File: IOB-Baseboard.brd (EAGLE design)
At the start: 106 x 100 mm, 21 parts

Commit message: added mounting holes
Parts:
- added U$3, U$4, U$5: MOUNTINGHOLE, SPCoast:MOUNTINGHOLE
- moved U$1 45.3 mm to (51.4, 85.2), turned to 0 degrees
- moved R18 11.5 mm to (6.22, 74.9), turned to 180 degrees
- moved LED18 9.25 mm to (6.22, 77.5)
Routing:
- net VIN: track 495.9 -> 484.3 mm
- net GND: track 45.1 -> 46.1 mm

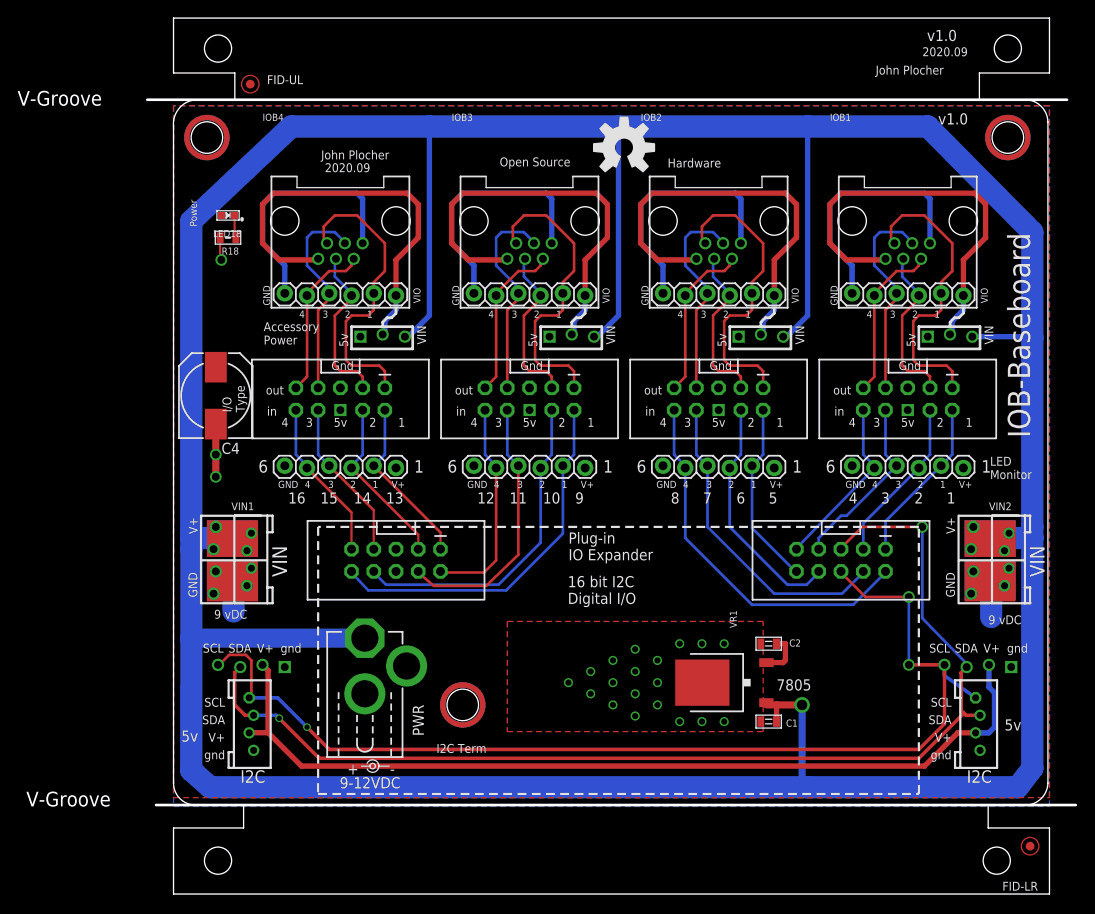
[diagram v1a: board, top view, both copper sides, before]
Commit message: put LEDS back on board, move 2x5 personal;ity and VIO connectors
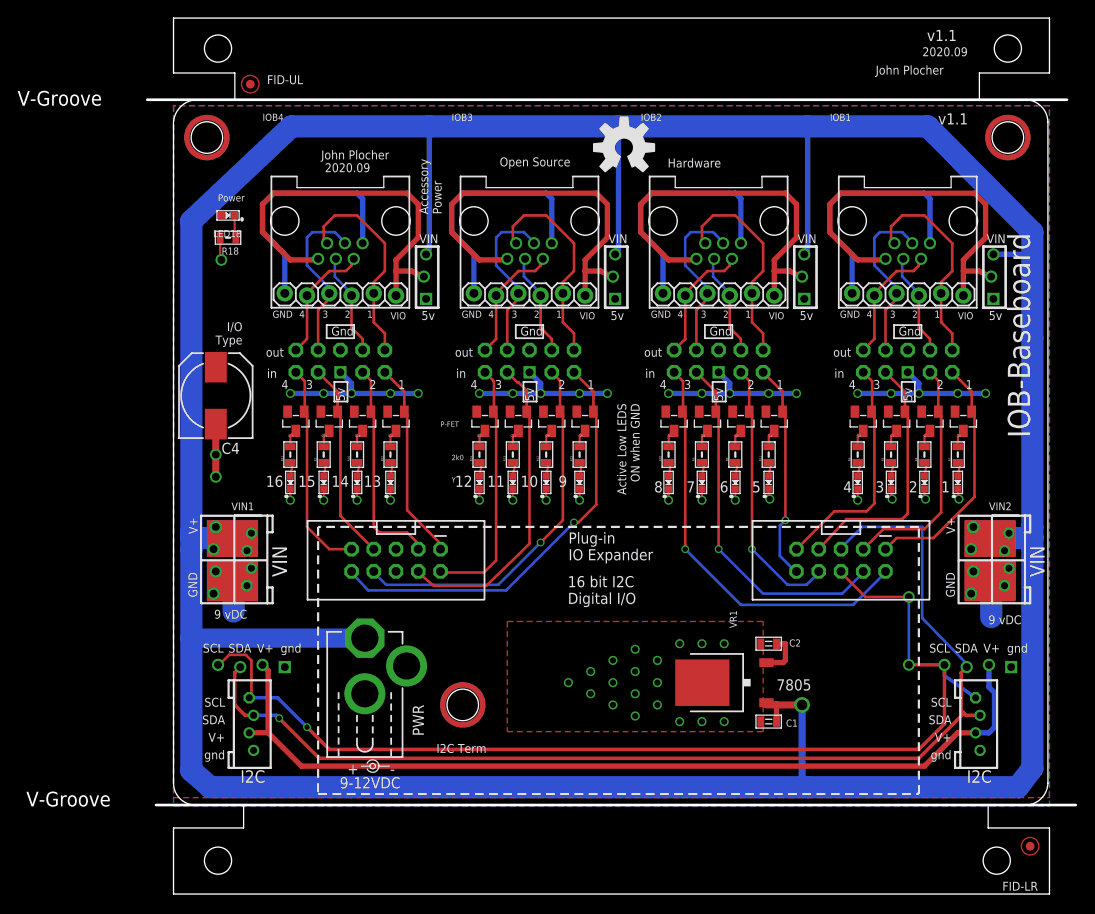
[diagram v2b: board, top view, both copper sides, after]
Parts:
- added LED10, LED11, LED12, LED13, LED14, LED15, LED17, LED19, LED2, LED3, LED4, LED5, LED6, LED7, LED8, LED9: Y, SPCoast:0603-LED
- added Q0, Q1, Q10, Q11, Q12, Q13, Q14, Q15, Q2, Q3, Q4, Q5, Q6, Q7, Q8, Q9: P-FET, SPCoast:SOT23
- added R10, R11, R12, R13, R14, R15, R16, R2, R21, R22, R4, R5, R6, R7, R8, R9: 2K0, SPCoast:0805-RES
- IOB1, IOB2, IOB3, IOB4: device SPCoast:IOB-V3 -> SPCoast:IOB-V3-BASE
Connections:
- new net N$10: LED8.A, R10.1
- new net N$11: Q8.3, R15.2
- new net N$12: Q9.3, R12.2
- new net N$13: Q10.3, R13.2
- new net N$14: Q11.3, R14.2
- new net N$15: LED13.A, R15.1
- new net N$16: LED10.A, R12.1
- new net N$23: LED11.A, R13.1
- new net N$24: LED12.A, R14.1
- new net N$28: Q12.3, R22.2
- new net N$29: Q13.3, R16.2
- new net N$3: Q4.3, R11.2
- new net N$30: Q14.3, R2.2
- new net N$31: Q15.3, R21.2
- new net N$32: LED19.A, R22.1
- new net N$33: LED14.A, R16.1
- new net N$34: LED15.A, R2.1
- new net N$35: LED17.A, R21.1
- new net N$4: Q5.3, R8.2
- new net N$44: Q0.3, R7.2
- new net N$45: Q1.3, R4.2
- new net N$46: Q2.3, R5.2
- new net N$47: Q3.3, R6.2
- new net N$48: LED5.A, R7.1
- new net N$49: LED2.A, R4.1
- new net N$5: Q6.3, R9.2
- new net N$50: LED3.A, R5.1
- new net N$51: LED4.A, R6.1
- new net N$6: Q7.3, R10.2
- new net N$7: LED9.A, R11.1
- new net N$8: LED6.A, R8.1
- new net N$9: LED7.A, R9.1
- net GND: now also LED10.C, LED11.C, LED12.C, LED13.C, LED14.C, LED15.C, LED17.C, LED19.C, LED2.C, LED3.C, LED4.C, LED5.C, LED6.C, LED7.C, LED8.C, LED9.C; no longer IOB1.GND@4, IOB2.GND@4, IOB3.GND@4, IOB4.GND@4
- net P1: now also Q0.1; no longer IOB1.I1@1
- net P10: now also Q9.1; no longer IOB3.I2@1
- net P11: now also Q10.1; no longer IOB3.I3@1
- net P12: now also Q11.1; no longer IOB3.I4@1
- net P13: now also Q12.1; no longer IOB4.I1@1
- net P14: now also Q13.1; no longer IOB4.I2@1
- net P15: now also Q14.1; no longer IOB4.I3@1
- net P16: now also Q15.1; no longer IOB4.I4@1
- net P2: now also Q1.1; no longer IOB1.I2@1
- net P3: now also Q2.1; no longer IOB1.I3@1
- net P4: now also Q3.1; no longer IOB1.I4@1
- net P5: now also Q4.1; no longer IOB2.I1@1
- net P6: now also Q5.1; no longer IOB2.I2@1
- net P7: now also Q6.1; no longer IOB2.I3@1
- net P8: now also Q7.1; no longer IOB2.I4@1
- net P9: now also Q8.1; no longer IOB3.I1@1
- net VCC: now also Q0.2, Q1.2, Q10.2, Q11.2, Q12.2, Q13.2, Q14.2, Q15.2, Q2.2, Q3.2, Q4.2, Q5.2, Q6.2, Q7.2, Q8.2, Q9.2; no longer IOB1.5V@4, IOB2.5V@4, IOB3.5V@4, IOB4.5V@4
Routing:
- net VCC: track 5.17 -> 80.8 mm, vias 0 -> 20
- net VIN: track 484.3 -> 459.9 mm
- net GND: track 46.1 -> 66.3 mm, vias 22 -> 38
- net P1: track 12.2 -> 27.9 mm
- net P3: track 13.6 -> 29.1 mm
- net P2: track 11.9 -> 27.2 mm
- net P4: track 13.0 -> 26.8 mm
- net P9: track 35.6 -> 49.2 mm, vias 0 -> 1
- net P16: track 11.4 -> 24.4 mm
- net P8: track 35.7 -> 48.2 mm, vias 0 -> 1
- net P10: track 30.3 -> 42.8 mm, vias 0 -> 1
- net P11: track 23.7 -> 36.0 mm
- net P14: track 12.4 -> 24.7 mm
- net P7: track 29.0 -> 41.0 mm, vias 0 -> 1
- net P12: track 17.5 -> 29.2 mm
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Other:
- board text added: "2k0"
- board text added: ">DRAWING_NAME"
- board text added: "Active Low LEDS ON when GND"
- board text added: "Made in the Coast Division, PCR, NMRA"
- board text added: "Model Railroading is Fun!"
- board text added: "P-FET"
- board text added: "Y"
- board text added: "v1.1"
- board text removed: "1.0 - experimental platform for plug in I/O interface, LED monitor and I2C chip carriers"
- board text removed: "5v"
- board text removed: "I2C-7313-IOB"
- board text removed: "LED Monitor"
- board text removed: "v1.0"

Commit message: update version text
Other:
- board text added: "v1.0"
- board text removed: "v1.1"
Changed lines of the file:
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@@
 <board>
 <plain>
-<text x="87.28339375" y="87.855534375" size="1.27" layer="21" rot="SR0">v1.1</text>
+<text x="87.28339375" y="87.855534375" size="1.27" layer="21" rot="SR0">v1.0</text>
 <text x="2.2548" y="40.2418" size="1.4224" layer="22" font="vector" ratio="15" rot="MR270">www. SP Coast .com</text>
 <text x="36.9627" y="83.2992" size="1.4224" layer="22" font="vector" ratio="15" rot="MR180">16 bit (4x IO4 ports)
@@
 <text x="45.085" y="38.1" size="1.27" layer="21" rot="SR0">Plug-in
 IO Expander</text>
-<text x="86.01339375" y="97.380534375" size="1.27" layer="21" rot="SR0">v1.1</text>
+<text x="86.01339375" y="97.380534375" size="1.27" layer="21" rot="SR0">v1.0</text>
 <text x="85.48799375" y="95.645009375" size="1.016" layer="21">2020.09</text>
 <text x="87.63" y="45.847" size="1.27" layer="21">1</text>

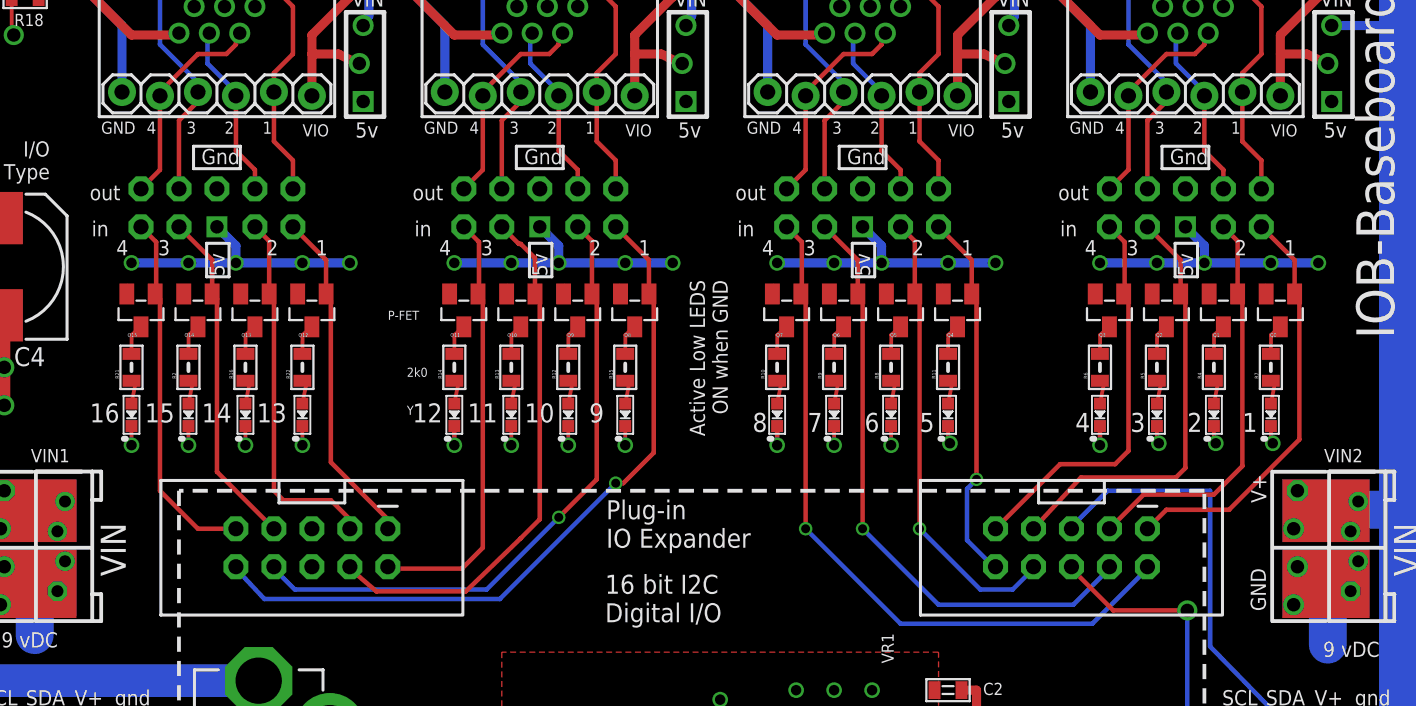
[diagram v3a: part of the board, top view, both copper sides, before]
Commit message: added values for connectors
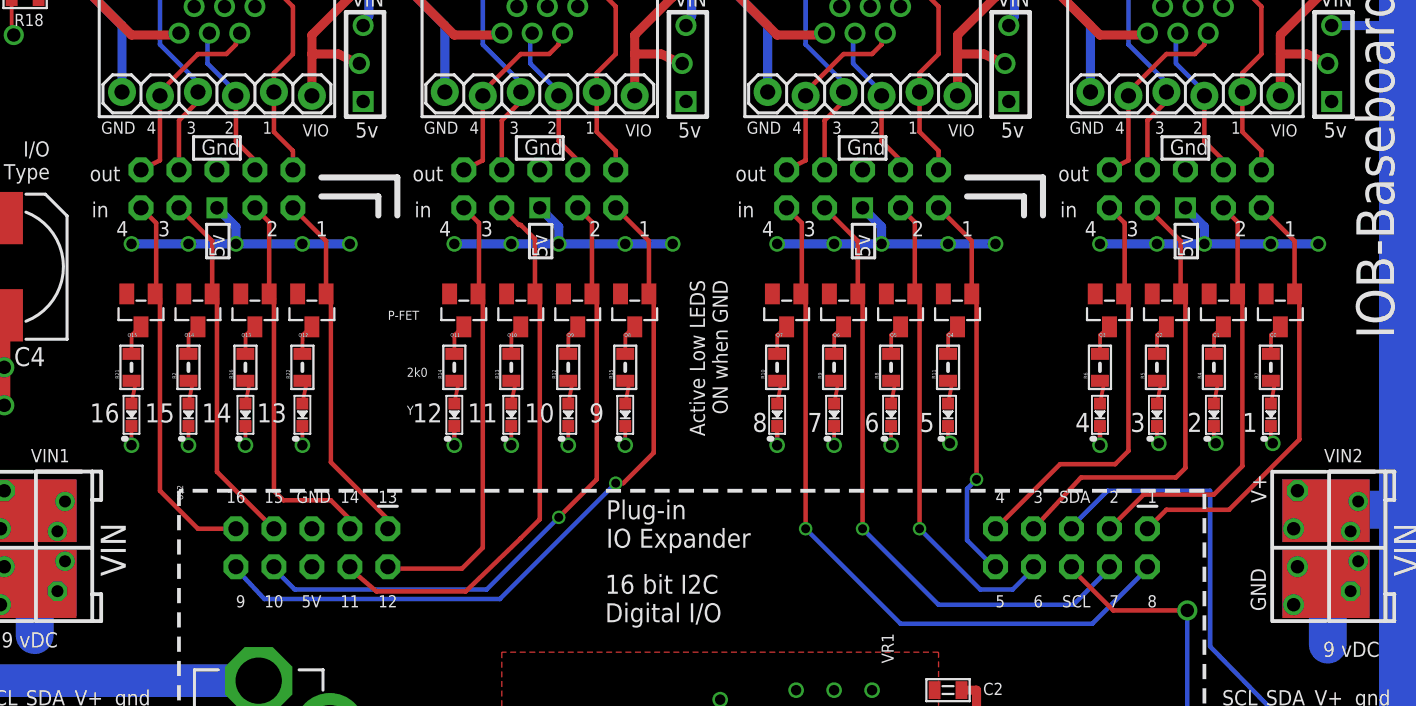
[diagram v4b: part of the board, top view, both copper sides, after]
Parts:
- J1, J2: value (none) -> I2C
- PWR: value (none) -> 2.1mm
- U$2: value I2C-EXPANDER -> CONNECTOR-I2C-EXPANDER
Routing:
- net P11: track 36.0 -> 37.3 mm
- net P10: track 42.8 -> 44.0 mm
- net P12: track 29.2 -> 30.5 mm
- net P9: track 49.2 -> 50.4 mm
- net P8: track 48.2 -> 49.5 mm
- net P7: track 41.0 -> 42.3 mm
- net P6: track 30.7 -> 32.0 mm
- net P5: track 24.9 -> 26.2 mm
- net P4: track 26.8 -> 28.1 mm
- net P3: track 29.1 -> 30.4 mm
- net P2: track 27.2 -> 28.4 mm
- net P16: track 24.4 -> 25.6 mm
- net P15: track 22.8 -> 24.1 mm
- net P14: track 24.7 -> 26.0 mm
- net P13: track 22.8 -> 24.1 mm
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
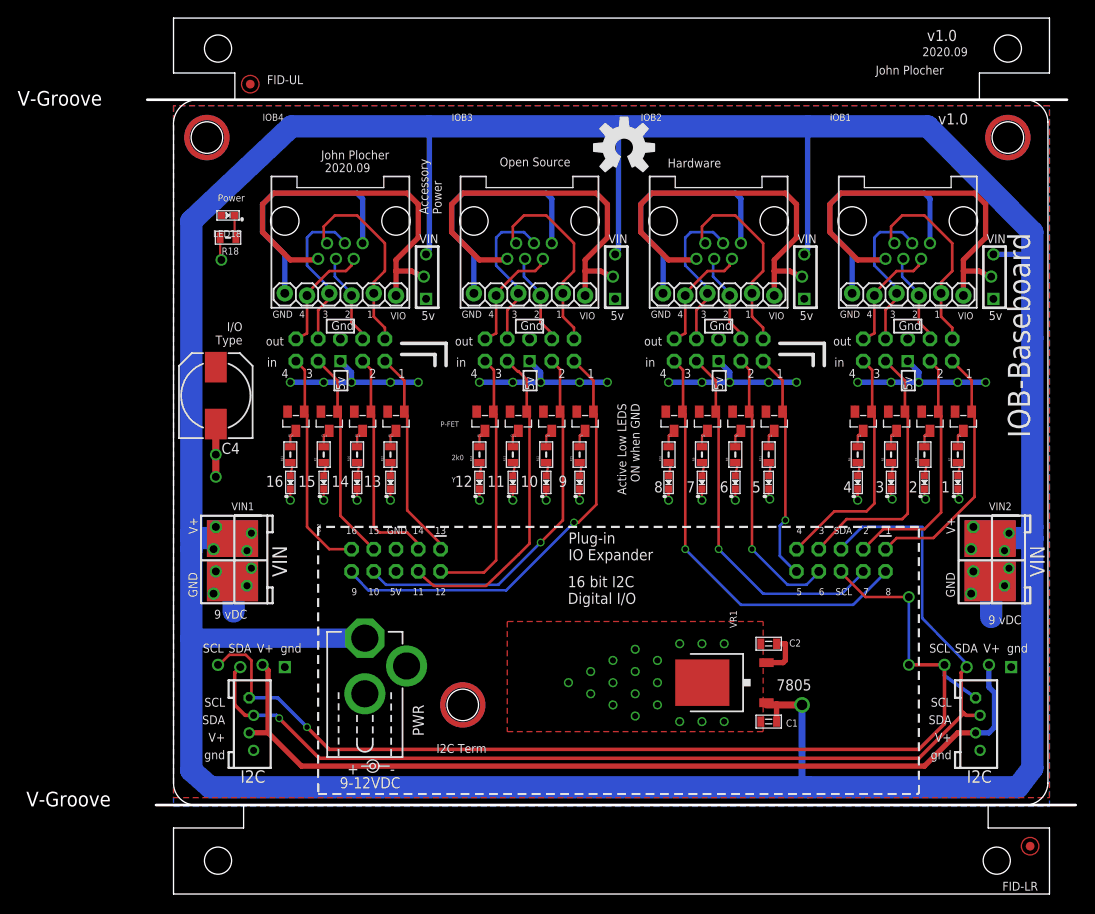
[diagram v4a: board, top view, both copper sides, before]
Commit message: normalized values
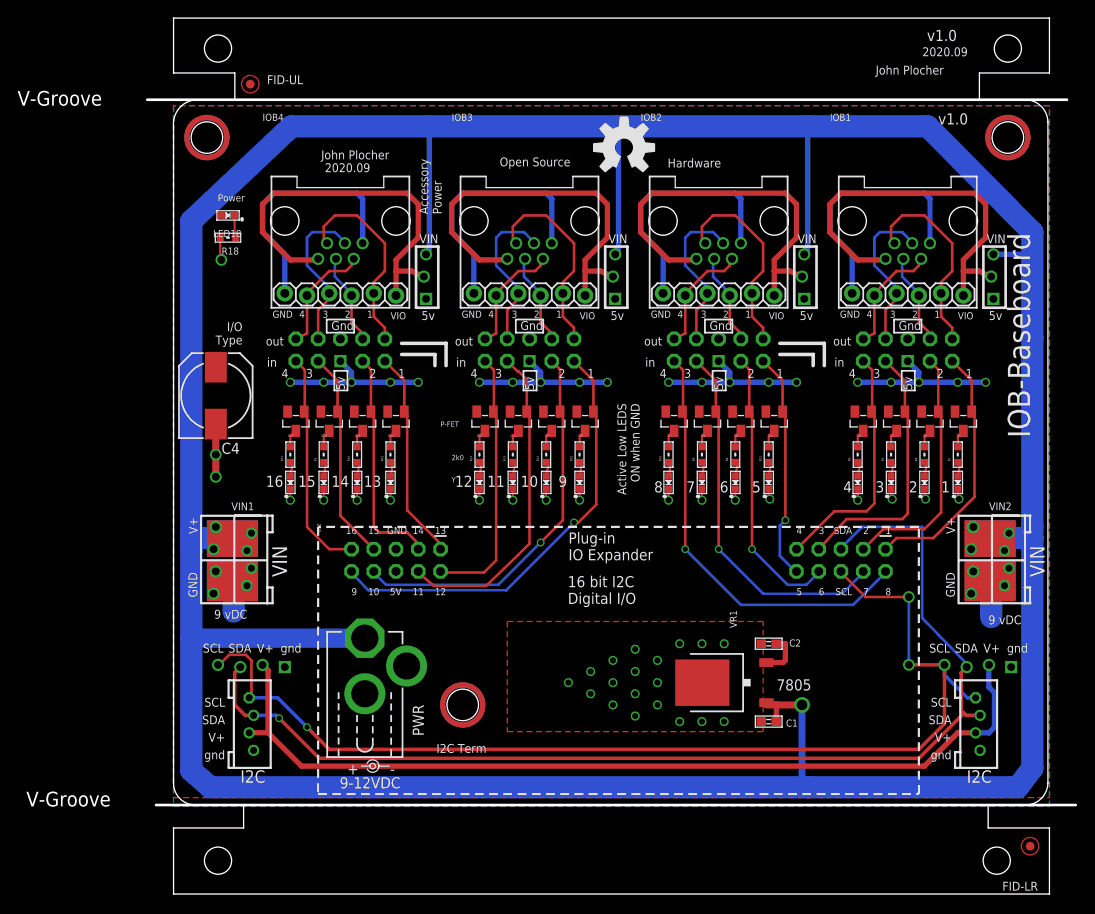
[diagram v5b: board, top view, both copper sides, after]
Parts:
- BOARD1: value BOARD80X100-IOB -> BOARD
- C1, C2: device SPCoast:0805-CAP -> SPCoast:0603-CAP
- IOB1, IOB2, IOB3, IOB4: value CONNECTOR-IO4-IOB-V3 -> CONNECTOR
- R10, R11, R12, R13, R14, R15, R16, R18, R2, R21, R22, R4, R5, R6, R7, R8, R9: device SPCoast:0805-RES -> SPCoast:0603-RES
- U$1: value OSHW-LOGOL -> OSHW
